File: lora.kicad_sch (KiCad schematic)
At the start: 7 parts, among them U11 RA-01SH

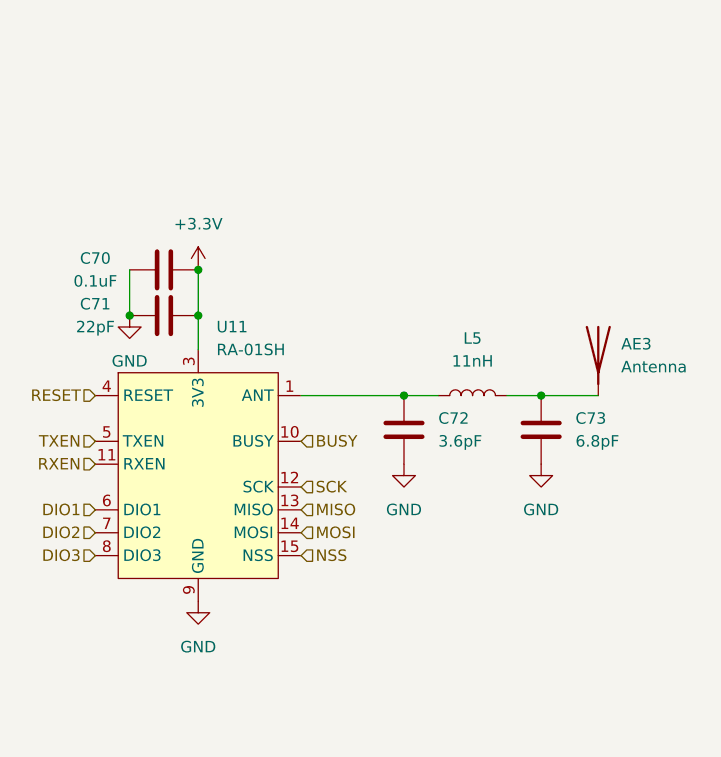
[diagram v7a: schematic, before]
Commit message: added nfc antenna components, added most of footprints
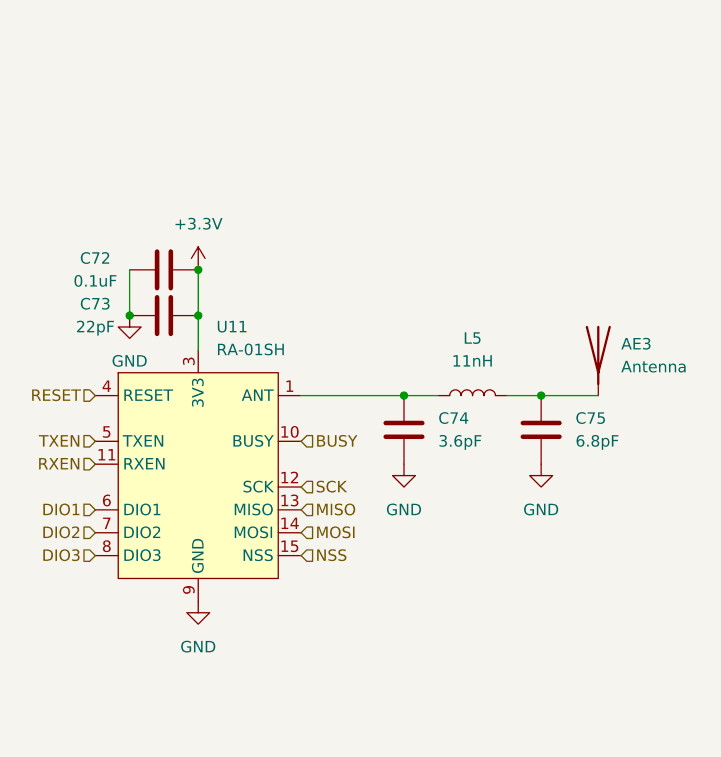
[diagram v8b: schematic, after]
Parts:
- AE3: footprint (none) -> airsoft_controller:LoRa-antenna-868-HESM
- C72: renamed from C70; footprint (none) -> Capacitor_SMD:C_0603_1608Metric_Pad1.08x0.95mm_HandSolder
- C73: renamed from C71; footprint (none) -> Capacitor_SMD:C_0603_1608Metric_Pad1.08x0.95mm_HandSolder
- C74: renamed from C72; footprint (none) -> Capacitor_SMD:C_0603_1608Metric_Pad1.08x0.95mm_HandSolder
- C75: renamed from C73; footprint (none) -> Capacitor_SMD:C_0603_1608Metric_Pad1.08x0.95mm_HandSolder
- U11: footprint (none) -> airsoft_controller:RA-01SH
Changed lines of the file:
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@@
   (symbol (lib_id "Device:C") (at 143.51 83.82 90) (unit 1)
     (in_bom yes) (on_board yes)
-    (property "Reference" "C71" (id 0) (at 135.89 82.55 90))
+    (property "Reference" "C73" (id 0) (at 135.89 82.55 90))
     (property "Value" "22pF" (id 1) (at 135.89 85.09 90))
-    (property "Footprint" "" (id 2) (at 147.32 82.8548 0)
+    (property "Footprint" "Capacitor_SMD:C_0603_1608Metric_Pad1.08x0.95mm_HandSolder" (id 2) (at 147.32 82.8548 0)
       (effects (font (size 1.27 1.27)) hide)
     )
@@
   (symbol (lib_id "Device:C") (at 185.42 96.52 0) (unit 1)
     (in_bom yes) (on_board yes) (fields_autoplaced)
-    (property "Reference" "C73" (id 0) (at 189.23 95.2499 0)
+    (property "Reference" "C75" (id 0) (at 189.23 95.2499 0)
       (effects (font (size 1.27 1.27)) (justify left))
     )
@@
       (effects (font (size 1.27 1.27)) (justify left))
     )
-    (property "Footprint" "" (id 2) (at 186.3852 100.33 0)
+    (property "Footprint" "Capacitor_SMD:C_0603_1608Metric_Pad1.08x0.95mm_HandSolder" (id 2) (at 186.3852 100.33 0)
       (effects (font (size 1.27 1.27)) hide)
     )
@@
       (effects (font (size 1.27 1.27)) (justify left))
     )
-    (property "Footprint" "" (id 2) (at 191.77 87.63 0)
+    (property "Footprint" "airsoft_controller:LoRa-antenna-868-HESM" (id 2) (at 191.77 87.63 0)
       (effects (font (size 1.27 1.27)) hide)
     )
@@
   (symbol (lib_id "Device:C") (at 143.51 78.74 90) (unit 1)
     (in_bom yes) (on_board yes)
-    (property "Reference" "C70" (id 0) (at 135.89 77.47 90))
+    (property "Reference" "C72" (id 0) (at 135.89 77.47 90))
     (property "Value" "0.1uF" (id 1) (at 135.89 80.01 90))
-    (property "Footprint" "" (id 2) (at 147.32 77.7748 0)
+    (property "Footprint" "Capacitor_SMD:C_0603_1608Metric_Pad1.08x0.95mm_HandSolder" (id 2) (at 147.32 77.7748 0)
       (effects (font (size 1.27 1.27)) hide)
     )
@@
   (symbol (lib_id "Device:C") (at 170.18 96.52 0) (unit 1)
     (in_bom yes) (on_board yes) (fields_autoplaced)
-    (property "Reference" "C72" (id 0) (at 173.99 95.2499 0)
+    (property "Reference" "C74" (id 0) (at 173.99 95.2499 0)
       (effects (font (size 1.27 1.27)) (justify left))
     )
@@
       (effects (font (size 1.27 1.27)) (justify left))
     )
-    (property "Footprint" "" (id 2) (at 171.1452 100.33 0)
+    (property "Footprint" "Capacitor_SMD:C_0603_1608Metric_Pad1.08x0.95mm_HandSolder" (id 2) (at 171.1452 100.33 0)
       (effects (font (size 1.27 1.27)) hide)
     )
@@
       (effects (font (size 1.27 1.27)) (justify left))
     )
-    (property "Footprint" "" (id 2) (at 147.32 101.6 0)
+    (property "Footprint" "airsoft_controller:RA-01SH" (id 2) (at 147.32 101.6 0)
       (effects (font (size 1.27 1.27)) hide)
     )
